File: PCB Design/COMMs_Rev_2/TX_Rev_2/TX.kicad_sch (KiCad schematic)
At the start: 54 parts, among them J1 Conn_01x24_Pin, J2 Conn_01x24_Pin, J3 Conn_01x03_Pin, J4 Conn_01x04_Pin, Q1 IPD50N10S3L16ATMA1, Q2 IPD50N10S3L16ATMA1, Q3 IPD50N10S3L16ATMA1, Q4 IPD50N10S3L16ATMA1, U1 UCC27211AQDDARQ1, U2 UCC27211AQDDARQ1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

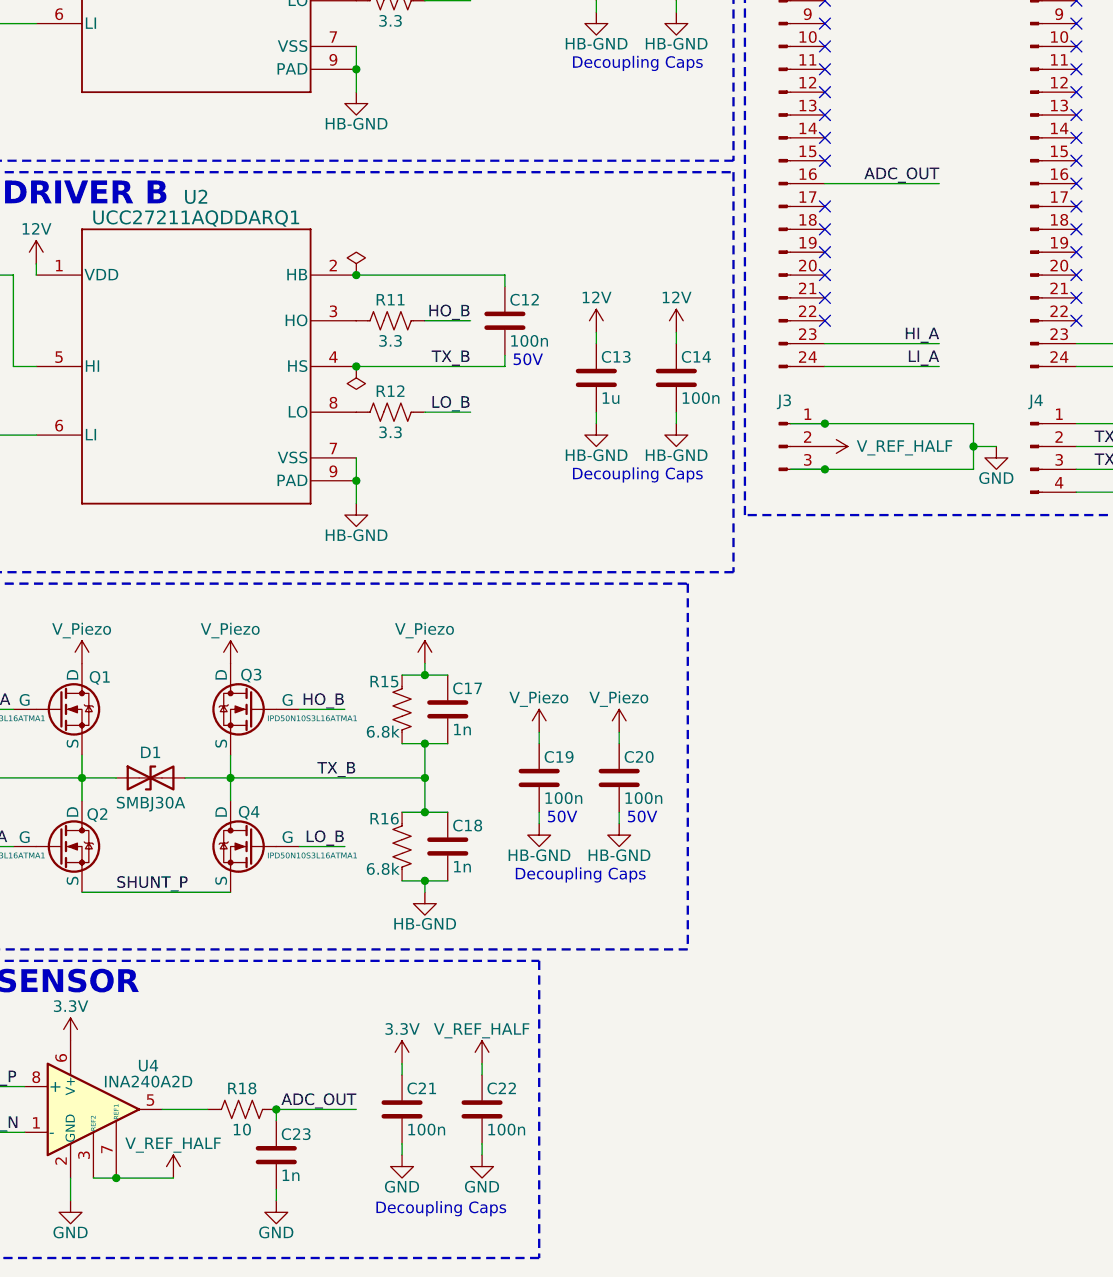
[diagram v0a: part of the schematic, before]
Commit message: Completed Initial PCB Component Placements
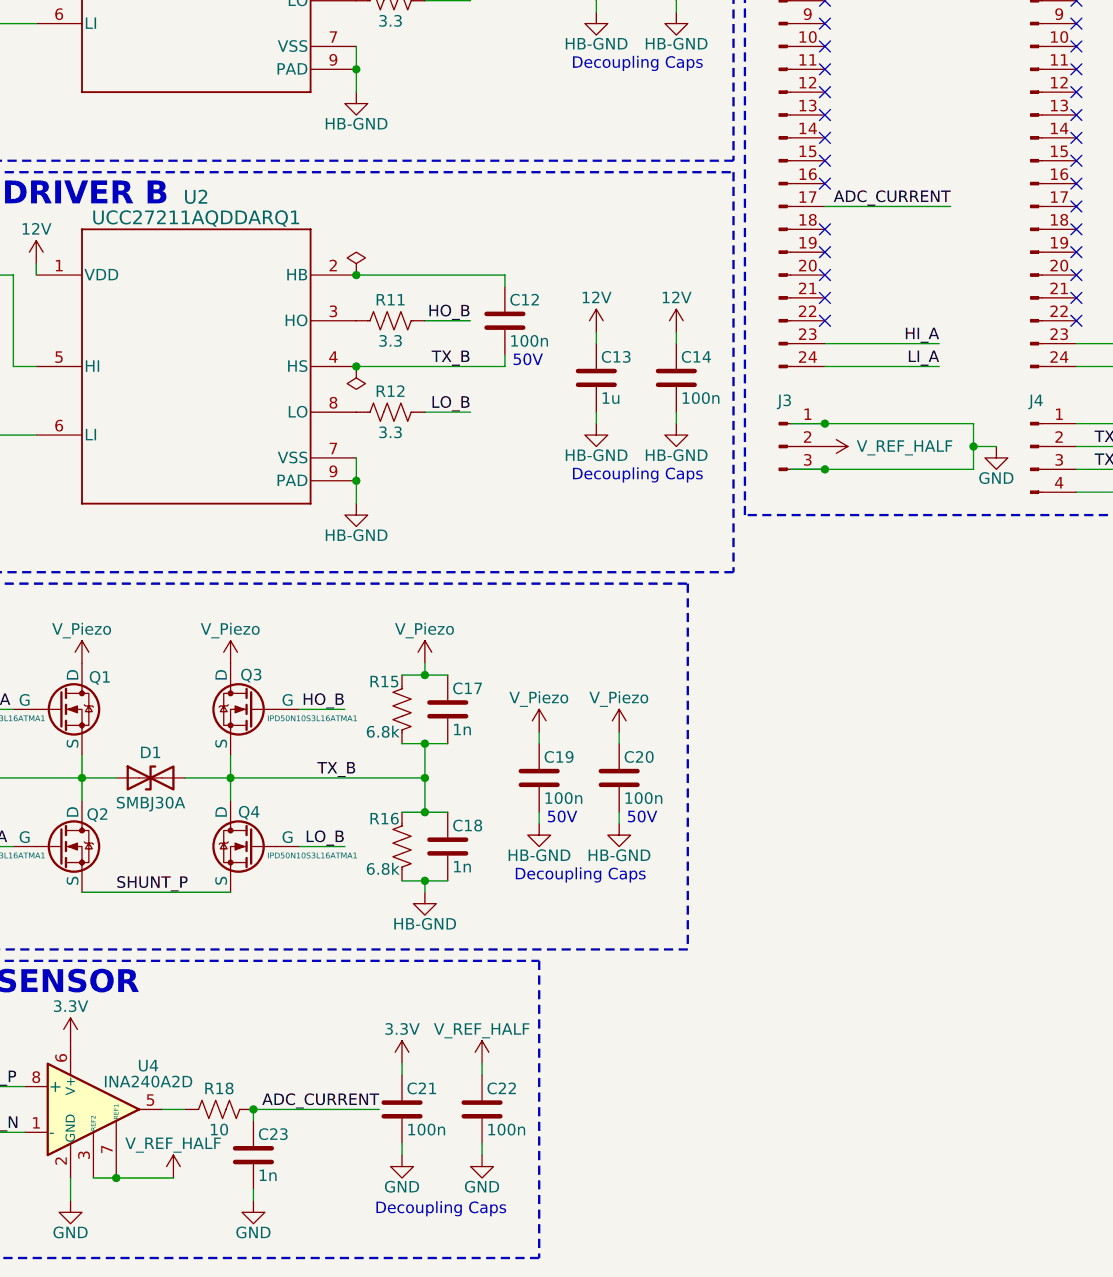
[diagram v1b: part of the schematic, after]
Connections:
- net ADC_CURRENT: now reaches J1.17 (Pin_17)
- net ADC_CURRENT: now also C23.1, R18.2
- removed net ADC_OUT: C23.1, J1.16 (Pin_16), R18.2
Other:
- moved on the sheet: C23, R18
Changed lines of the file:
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@@
 	)
 	(junction
-		(at 81.28 123.19)
+		(at 62.23 163.83)
 		(diameter 0)
 		(color 0 0 0 0)
 	)
 	(junction
-		(at 29.21 43.18)
+		(at 81.28 123.19)
 		(diameter 0)
 		(color 0 0 0 0)
 	)
 	(junction
-		(at 21.59 138.43)
+		(at 29.21 43.18)
 		(diameter 0)
 		(color 0 0 0 0)
 	)
 	(junction
-		(at 24.13 171.45)
+		(at 21.59 138.43)
 		(diameter 0)
 		(color 0 0 0 0)
 	)
 	(junction
-		(at 64.77 163.83)
+		(at 24.13 171.45)
 		(diameter 0)
 		(color 0 0 0 0)
@@
 	)
 	(no_connect
+		(at 125.73 60.96)
+	)
+	(no_connect
 		(at 153.67 43.18)
 	)
@@
 	)
 	(no_connect
-		(at 125.73 63.5)
-	)
-	(no_connect
 		(at 125.73 43.18)
 	)
@@
 	(wire
 		(pts
-			(xy 64.77 165.1) (xy 64.77 163.83)
+			(xy 62.23 165.1) (xy 62.23 163.83)
 		)
 		(stroke
@@
 	(wire
 		(pts
+			(xy 125.73 63.5) (xy 139.7 63.5)
+		)
+		(stroke
+			(width 0)
+			(type default)
+		)
+	)
+	(wire
+		(pts
 			(xy 21.59 130.81) (xy 19.05 130.81)
 		)
@@
 	(wire
 		(pts
+			(xy 62.23 163.83) (xy 76.2 163.83)
+		)
+		(stroke
+			(width 0)
+			(type default)
+		)
+	)
+	(wire
+		(pts
 			(xy 81.28 86.36) (xy 86.36 86.36)
 		)
@@
 	(wire
 		(pts
-			(xy 64.77 172.72) (xy 64.77 173.99)
+			(xy 62.23 172.72) (xy 62.23 173.99)
 		)
 		(stroke
@@
 	(wire
 		(pts
-			(xy 64.77 163.83) (xy 73.66 163.83)
-		)
-		(stroke
-			(width 0)
-			(type default)
-		)
-	)
-	(wire
-		(pts
 			(xy 81.28 138.43) (xy 83.82 138.43)
 		)
@@
 	(wire
 		(pts
-			(xy 52.07 163.83) (xy 57.15 163.83)
+			(xy 52.07 163.83) (xy 54.61 163.83)
 		)
 		(stroke
@@
 	(wire
 		(pts
-			(xy 125.73 60.96) (xy 138.43 60.96)
-		)
-		(stroke
-			(width 0)
-			(type default)
-		)
-	)
-	(wire
-		(pts
 			(xy 30.48 119.38) (xy 35.56 119.38)
 		)
@@
 		)
 	)
+	(label "ADC_CURRENT"
+		(at 139.7 63.5 180)
+		(effects
+			(font
+				(size 1.27 1.27)
+			)
+			(justify right bottom)
+		)
+	)
 	(label "SHUNT_P"
 		(at 15.24 158.75 0)
@@
 		)
 	)
-	(label "ADC_OUT"
-		(at 73.66 163.83 180)
-		(effects
-			(font
-				(size 1.27 1.27)
-			)
-			(justify right bottom)
-		)
-	)
 	(label "LI_B"
 		(at 165.1 81.28 180)
@@
 		)
 	)
-	(label "ADC_OUT"
-		(at 138.43 60.96 180)
+	(label "TX_A"
+		(at 29.21 127 0)
 		(effects
 			(font
 				(size 1.27 1.27)
 			)
-			(justify right bottom)
+			(justify left bottom)
 		)
 	)
-	(label "TX_A"
-		(at 29.21 127 0)
+	(label "LO_A"
+		(at 86.36 40.64 180)
 		(effects
 			(font
 				(size 1.27 1.27)
 			)
-			(justify left bottom)
+			(justify right bottom)
 		)
 	)
-	(label "LO_A"
-		(at 86.36 40.64 180)
+	(label "ADC_CURRENT"
+		(at 76.2 163.83 180)
 		(effects
 			(font
@@
 	(symbol
 		(lib_id "Device:C")
-		(at 64.77 168.91 0)
+		(at 62.23 168.91 0)
 		(unit 1)
 		(exclude_from_sim no)
@@
 		(dnp no)
 		(property "Reference" "C23"
-			(at 65.278 166.624 0)
+			(at 62.738 166.624 0)
 			(effects
 				(font
@@
 		)
 		(property "Value" "1n"
-			(at 65.278 171.196 0)
+			(at 62.738 171.196 0)
 			(effects
 				(font
@@
 		)
 		(property "Footprint" "Capacitor_SMD:C_0603_1608Metric"
-			(at 65.7352 172.72 0)
+			(at 63.1952 172.72 0)
 			(effects
 				(font
@@
 		)
 		(property "Datasheet" "~"
-			(at 64.77 168.91 0)
+			(at 62.23 168.91 0)
 			(effects
 				(font
@@
 		)
 		(property "Description" "Unpolarized capacitor"
-			(at 64.77 168.91 0)
+			(at 62.23 168.91 0)
 			(effects
 				(font
@@
 	(symbol
 		(lib_id "power:GND")
-		(at 64.77 173.99 0)
+		(at 62.23 173.99 0)
 		(unit 1)
 		(exclude_from_sim no)
@@
 		(dnp no)
 		(property "Reference" "#PWR053"
-			(at 64.77 180.34 0)
+			(at 62.23 180.34 0)
 			(effects
 				(font
@@
 		)
 		(property "Value" "GND"
-			(at 64.77 177.546 0)
+			(at 62.23 177.546 0)
 			(effects
 				(font
@@
 		)
 		(property "Footprint" ""
-			(at 64.77 173.99 0)
+			(at 62.23 173.99 0)
 			(effects
 				(font
@@
 		)
 		(property "Datasheet" ""
-			(at 64.77 173.99 0)
+			(at 62.23 173.99 0)
 			(effects
 				(font
@@
 		)
 		(property "Description" "Power symbol creates a global label with name \"GND\" , ground"
-			(at 64.77 173.99 0)
+			(at 62.23 173.99 0)
 			(effects
 				(font
@@
 		(on_board yes)
 		(dnp no)
-		(property "Reference" "#PWR064"
+		(property "Reference" "#PWR0101"
 			(at 166.37 97.79 0)
 			(effects
@@
 			(project "TX"
 				(path "/db628952-7712-4c33-95ca-df895d26f0e8"
-					(reference "#PWR064")
+					(reference "#PWR0101")
 					(unit 1)
 				)
@@
 	(symbol
 		(lib_id "Device:R_US")
-		(at 60.96 163.83 90)
+		(at 58.42 163.83 90)
 		(unit 1)
 		(exclude_from_sim no)
@@
 		(dnp no)
 		(property "Reference" "R18"
-			(at 60.96 161.544 90)
+			(at 58.42 161.544 90)
 			(effects
 				(font
@@
 		)
 		(property "Value" "10"
-			(at 60.96 166.116 90)
+			(at 58.42 166.116 90)
 			(effects
 				(font
@@
 		)
 		(property "Footprint" "Resistor_SMD:R_0603_1608Metric"
-			(at 61.214 162.814 90)
+			(at 58.674 162.814 90)
 			(effects
 				(font
@@
 		)
 		(property "Datasheet" "~"
-			(at 60.96 163.83 0)
+			(at 58.42 163.83 0)
 			(effects
 				(font
@@
 		)
 		(property "Description" "Resistor, US symbol"
-			(at 60.96 163.83 0)
+			(at 58.42 163.83 0)
 			(effects
 				(font
